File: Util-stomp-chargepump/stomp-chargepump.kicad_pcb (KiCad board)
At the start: 2 copper layers, 52.7 x 28.6 mm, 12 parts, among them J1 1x8, U1 ICL7660

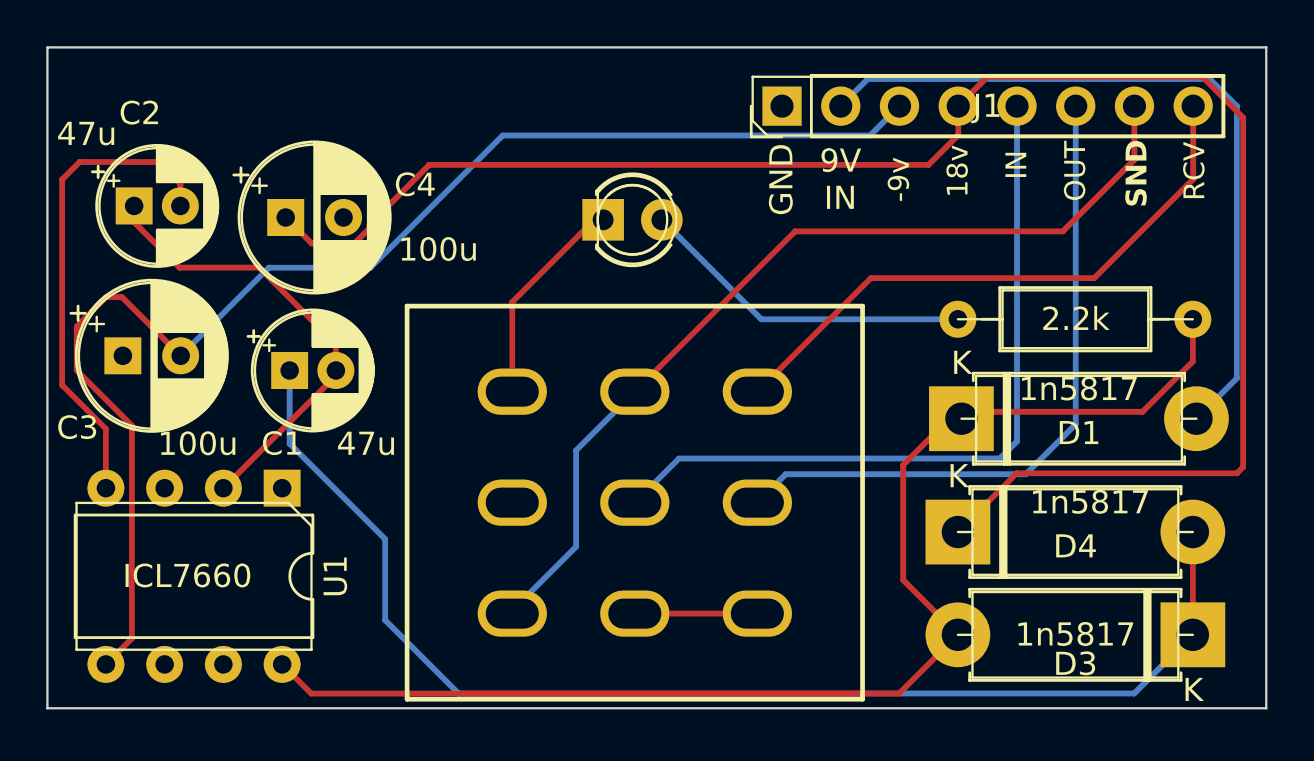
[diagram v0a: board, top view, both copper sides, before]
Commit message: added tweed57 overdrive
updated layout of the chargepump pcb
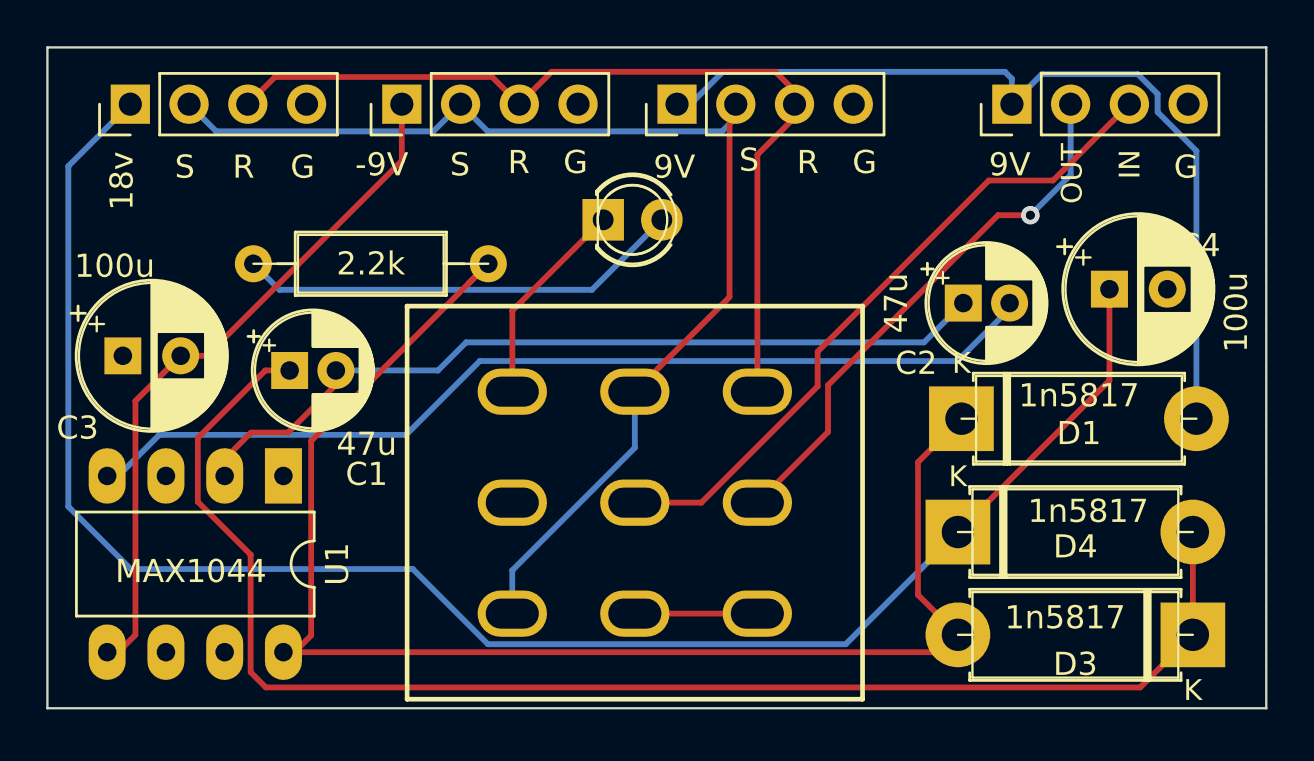
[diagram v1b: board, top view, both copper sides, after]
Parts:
- added J2: to-effect, Connector_PinHeader_2.54mm:PinHeader_1x04_P2.54mm_Vertical, F.Cu at (103.3, 70.4)
- added J3: from-top-jacks, Connector_PinHeader_2.54mm:PinHeader_1x04_P2.54mm_Vertical, F.Cu at (141.4, 70.4)
- added J4: to-effect, Connector_PinHeader_2.54mm:PinHeader_1x04_P2.54mm_Vertical, F.Cu at (126.9, 70.4)
- J1: value 1x8 -> to-effect; footprint Connector_PinHeader_2.54mm:PinHeader_1x08_P2.54mm_Vertical -> Connector_PinHeader_2.54mm:PinHeader_1x04_P2.54mm_Vertical
- U1: value ICL7660 -> MAX1044; footprint Package_DIP:DIP-8_W7.62mm -> Package_DIP:DIP-8_W7.62mm_LongPads
- moved C2 36.1 mm to (139.3, 79.0)
- moved C4 35.8 mm to (145.6, 78.4)
- moved R1 30.6 mm to (118.8, 77.3)
- moved J1 16.4 mm to (115.0, 70.4)
- moved U1 0.53 mm to (109.9, 86.5)
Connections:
- J1 pad 1: GND -> -9V
- J1 pad 2: +9V -> SEND
- J1 pad 3: -9V -> RECV
- J1 pad 4: 18V -> GND
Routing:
- net -9V: track 57.7 -> 30.2 mm
- net Net-(U1-CAP-): track 20.9 -> 42.5 mm
- net Net-(U1-CAP+): track 19.1 -> 36.4 mm
- net RECV: track 25.8 -> 39.7 mm
- net SEND: track 39.9 -> 52.4 mm
- net Net-(D3-K): track 54.2 -> 62.7 mm
- net Net-(D1-K): track 55.3 -> 62.8 mm
- net OUT: track 29.4 -> 23.7 mm, vias 0 -> 1
- net +9V: track 32.3 -> 37.6 mm
- net Net-(D2-A): track 15.2 -> 19.4 mm
- net IN: track 32.1 -> 29.4 mm
- net unconnected-(U1-NC-Pad1): track 0.65 -> 0.00 mm
- net Net-(D2-K): track 9.57 -> 9.06 mm
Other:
- board text added: "-9V"
- board text added: "9V"
- board text added: "G"
- board text added: "R"
- board text added: "S"
- board text removed: "-9v"
- board text removed: "9V IN"
- board text removed: "GND"
- board text removed: "RCV"
- board text removed: "SND"
